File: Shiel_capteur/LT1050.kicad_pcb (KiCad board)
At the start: 2 copper layers, 68.6 x 53.3 mm, 22 parts, among them P1 Power, P2 Analog, P3 Digital, P4 Digital, P5 CONN_01X01, P6 CONN_01X01, P7 CONN_01X01, P8 CONN_01X01, U0 Capteur_graphite, U1 LT1050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

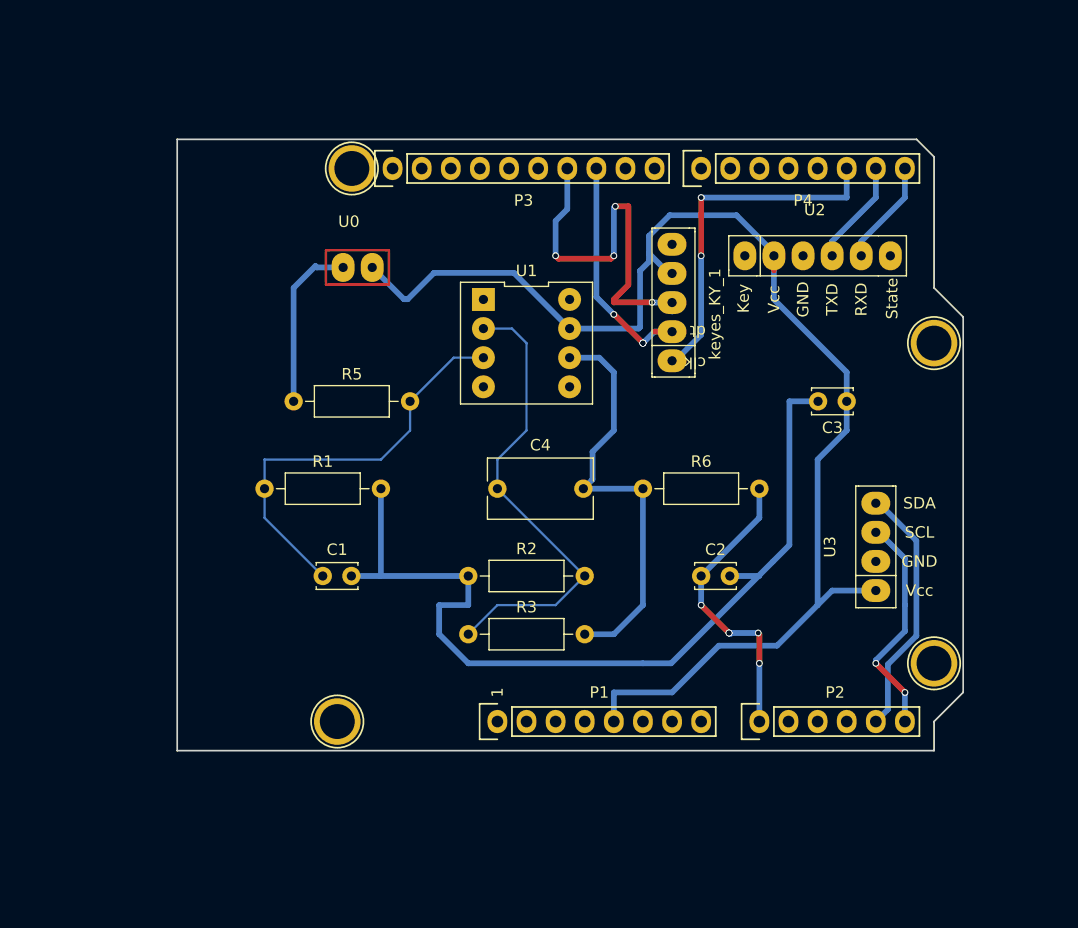
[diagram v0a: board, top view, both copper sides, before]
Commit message: correction routage
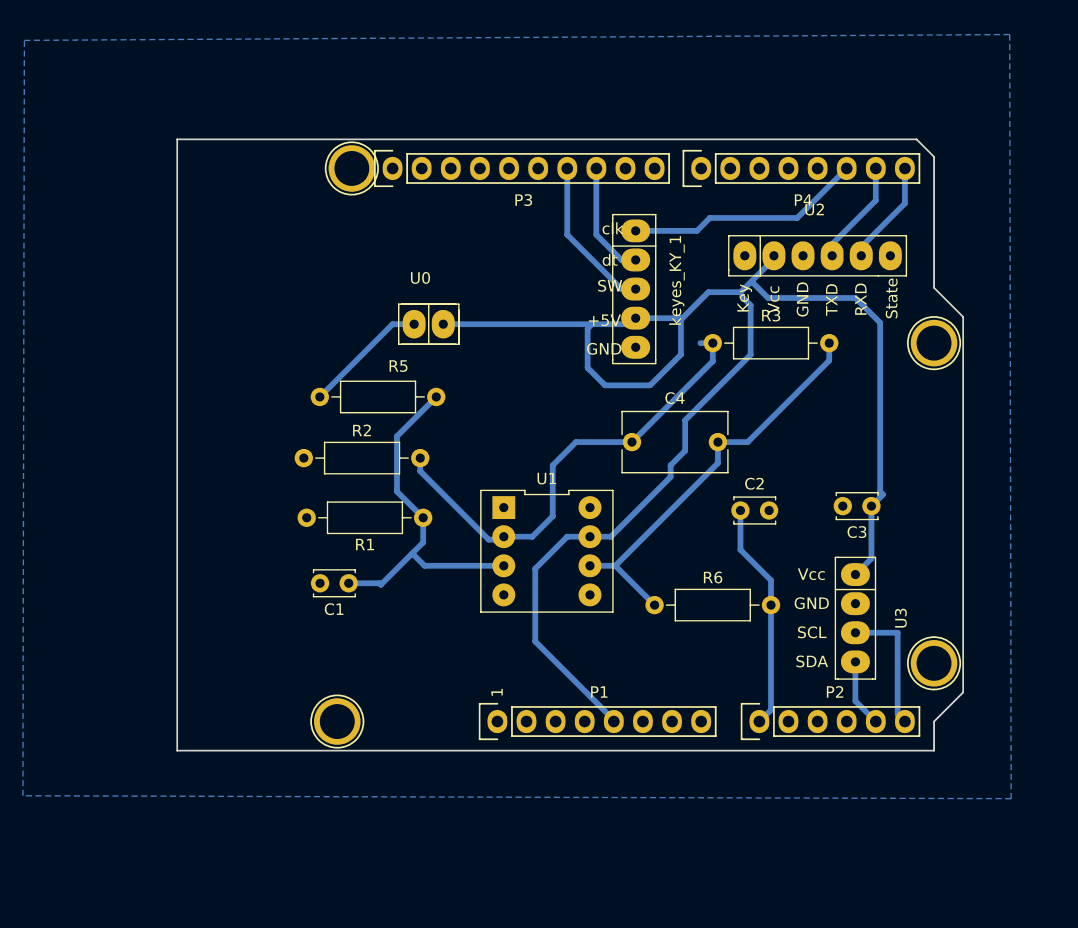
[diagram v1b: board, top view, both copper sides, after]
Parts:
- keyes_KY_1: value Encodeur_rotatoire -> Encodeur
- moved R3 33.2 mm to (157.7, 90.8)
- moved U1 18.2 mm to (143.3, 109.0)
- moved R2 17.7 mm to (122.0, 100.8)
- moved R1 14.1 mm to (132.5, 106.0), turned to 180 degrees
- moved C4 12.4 mm to (150.7, 99.4)
- moved R6 10.2 mm to (152.7, 113.7)
- moved C3 9.40 mm to (171.6, 105.0)
- moved U0 7.97 mm to (132.7, 89.2)
- moved C2 6.66 mm to (160.1, 105.4)
- moved U3 6.47 mm to (170.2, 114.8), turned to -90 degrees
- moved keyes_KY_1 4.49 mm to (151.0, 85.1), turned to -90 degrees
- moved C1 2.35 mm to (126.0, 111.8), turned to 180 degrees
- moved R5 2.32 mm to (123.4, 95.5)
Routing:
- net GND: track 79.0 -> 0.00 mm
- net SW: track 33.6 -> 13.7 mm, vias 4 -> 0
- net +5V: track 116.3 -> 134.5 mm
- net SDA: track 22.1 -> 5.94 mm
- net DT: track 21.5 -> 10.1 mm, vias 4 -> 0
- net CLK: track 30.7 -> 20.7 mm, vias 2 -> 0
- net SCL: track 19.8 -> 11.7 mm, vias 2 -> 0
- net ADC: track 26.3 -> 19.9 mm, vias 5 -> 0
- net IN+: track 36.5 -> 31.6 mm
- net capteur: track 15.1 -> 10.9 mm
- net /6: track 37.1 -> 35.7 mm
- added copper zone on B.Cu, net GND

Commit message: ajout tracerkicad
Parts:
- moved U3 10.9 mm to (169.8, 103.9)
- moved C3 9.67 mm to (170.9, 95.4)
- moved keyes_KY_1 5.98 mm to (145.7, 87.9)
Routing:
- net SDA: track 5.94 -> 17.0 mm
- net SCL: track 11.7 -> 21.7 mm
- net +5V: track 134.5 -> 124.7 mm
- net CLK: track 20.7 -> 27.1 mm
- net SW: track 13.7 -> 19.0 mm
- net DT: track 10.1 -> 15.1 mm

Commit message: mise à jour pcb
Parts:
- keyes_KY_1: value Encodeur -> Encodeur_rotatoire
- moved U2 36.5 mm to (130.4, 83.6)
- moved keyes_KY_1 5.70 mm to (142.0, 92.2)
- moved U0 0.72 mm to (133.2, 88.6)
- moved U3 0.25 mm to (170.1, 103.9)
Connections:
- P3 pad 7: SW -> TXD
- P3 pad 8: DT -> RXD
- P4 pad 3: /5(**) -> SW
- P4 pad 4: /4 -> DT
- P4 pad 7: TXD -> unconnected-(P4-Pad7)
- P4 pad 8: RXD -> unconnected-(P4-Pad8)
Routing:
- net DT: track 15.1 -> 35.7 mm
- net SW: track 19.0 -> 38.7 mm
- net RXD: track 9.20 -> 17.4 mm
- net TXD: track 9.20 -> 17.4 mm
- net +5V: track 124.7 -> 118.8 mm
- net CLK: track 27.1 -> 32.6 mm
- net SCL: track 21.7 -> 23.3 mm
- net IN+: track 31.6 -> 31.0 mm

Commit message: correction cathy
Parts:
- C4: footprint Capacitor_THT:C_Rect_L9.0mm_W5.1mm_P7.50mm_MKT -> Capacitor_THT:C_Rect_L7.5mm_W6.5mm_P5.00mm
- moved U0 5.80 mm to (127.6, 90.2)
- moved R5 5.34 mm to (118.1, 95.4)
- moved U2 5.34 mm to (125.1, 83.4)
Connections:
- P3 pad 10: /8 -> unconnected-(P3-Pad10)
- P3 pad 5: /13(SCK) -> unconnected-(P3-Pad5)
- P3 pad 6: /12(MISO) -> unconnected-(P3-Pad6)
- P4 pad 1: /7 -> unconnected-(P4-Pad1)
- P4 pad 2: /6(**) -> unconnected-(P4-Pad2)
- P4 pad 5: /3(**) -> unconnected-(P4-Pad5)
- U3 pad 1: +5V -> GND
- U3 pad 2: GND -> +5V
- keyes_KY_1 pad 5: unconnected-(keyes_KY_1-Pad5) -> GND
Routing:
- net +5V: track 118.8 -> 126.2 mm
- net RXD: track 17.4 -> 24.1 mm
- net SW: track 38.7 -> 44.9 mm
- net TXD: track 17.4 -> 23.5 mm
- net CLK: track 32.6 -> 35.9 mm
- net /6: track 35.7 -> 38.8 mm
- net IN-: track 41.0 -> 39.2 mm
- net IN+: track 31.0 -> 29.4 mm
- net SCL: track 23.3 -> 22.1 mm
- net capteur: track 10.9 -> 9.82 mm
- net SDA: track 17.0 -> 18.0 mm
- net DT: track 35.7 -> 36.6 mm

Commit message: ajout ltspice
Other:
- board text added: "PCB Diane_Thomas 2021-2022"
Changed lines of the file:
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@@
     (fp_line (start 3.55 1.5) (end -2.25 1.5) (layer "F.CrtYd") (width 0.05))
     (fp_line (start 3.55 1.3) (end 3.55 -1.3) (layer "F.CrtYd") (width 0.05))
-    (pad "1" thru_hole circle (at -1 0 180) (size 2.54 2.54) (drill 0.8) (layers *.Cu *.Mask)
+    (pad "1" thru_hole circle (at -0.75 0 180) (size 2.54 2.54) (drill 0.8) (layers *.Cu *.Mask)
       (net 6 "IN+") (pintype "passive"))
     (pad "2" thru_hole circle (at 2.25 0 180) (size 2.54 2.54) (drill 0.8) (layers *.Cu *.Mask)
       (net 4 "GND") (pintype "passive"))
     (model "${KICAD6_3DMODEL_DIR}/Capacitor_THT.3dshapes/C_Disc_D3.4mm_W2.1mm_P2.50mm.wrl"
-      (offset (xyz 0 0 0))
+      (offset (xyz -0.5 0 0))
       (scale (xyz 1 1 1))
       (rotate (xyz 0 0 0))
@@
   (gr_line (start 175.514 73.025) (end 110.998 73.025) (layer "Edge.Cuts") (width 0.15))
   (gr_line (start 177.038 85.979) (end 177.038 74.549) (layer "Edge.Cuts") (width 0.15))
+  (gr_text "PCB\nDiane_Thomas\n2021-2022" (at 118.745 116.967) (layer "B.Cu")
+    (effects (font (size 1.5 1.5) (thickness 0.3)))
+  )
   (gr_text "1" (at 138.938 121.285 90) (layer "F.SilkS")
     (effects (font (size 1 1) (thickness 0.15)))

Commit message: mise à jour correction kicad Cathy
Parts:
- moved R3 7.19 mm to (152.8, 96.0)
- moved C1 5.91 mm to (126.9, 117.6)
- moved C2 5.88 mm to (160.8, 111.3)
- moved C4 5.69 mm to (155.5, 102.5)
- moved R5 5.64 mm to (121.4, 99.9)
- moved R1 5.36 mm to (132.0, 111.4)
- moved U2 4.75 mm to (126.4, 88.0)
- moved R2 4.74 mm to (121.4, 105.5)
- moved U0 4.21 mm to (127.2, 94.4)
- moved R6 3.95 mm to (152.9, 117.6)
- moved U1 3.83 mm to (143.6, 112.8)
- moved C3 1.89 mm to (171.6, 93.6)
- moved U3 1.17 mm to (171.2, 104.1)
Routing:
- net +5V: track 126.2 -> 115.3 mm
- net /6: track 38.8 -> 32.7 mm
- net ADC: track 19.9 -> 14.5 mm
- net RXD: track 24.1 -> 28.6 mm
- net CLK: track 35.9 -> 40.1 mm
- net IN+: track 29.4 -> 33.3 mm
- net SCL: track 22.1 -> 25.4 mm
- net capteur: track 9.82 -> 6.56 mm
- net DT: track 36.6 -> 39.8 mm
- net IN-: track 39.2 -> 42.1 mm
- net TXD: track 23.5 -> 26.1 mm
- net SW: track 44.9 -> 42.7 mm
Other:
- board text added: "PCB Diane Thomas"
- board text removed: "PCB Diane_Thomas 2021-2022"
